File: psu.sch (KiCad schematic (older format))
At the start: 13 parts

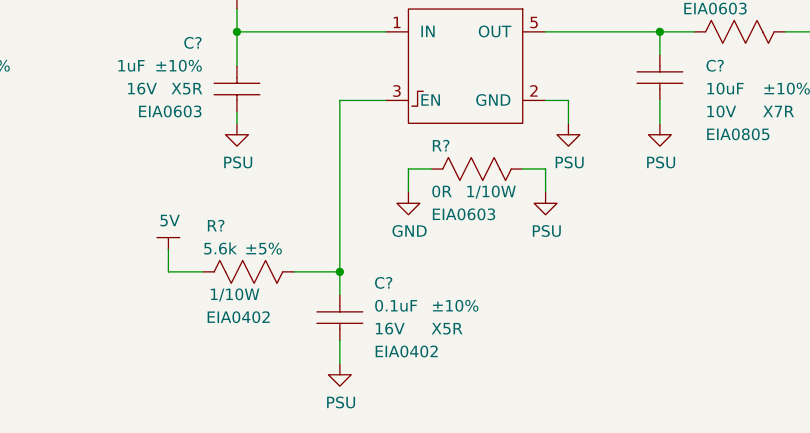
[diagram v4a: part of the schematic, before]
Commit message: Update ceramic capacitors with Vendor, Vendor_Pn, Fit fields following master library update.
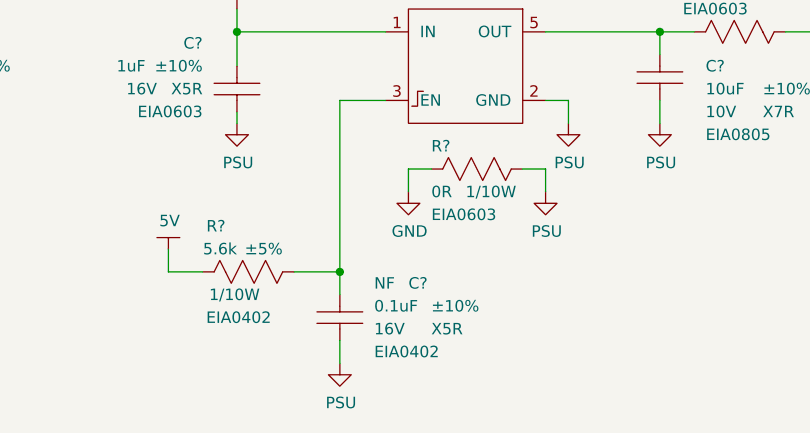
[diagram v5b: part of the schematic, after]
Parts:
- C? (x2): Digi-Key_PN 399-C0603C105K4PAC7411CT-ND -> (none); Fit (none) -> Yes; Vendor (none) -> Digikey; Vendor_PN (none) -> 399-C0603C105K4PAC7411CT-ND
- C?: Digi-Key_PN 399-14941-1-ND -> (none); Fit (none) -> Yes; Vendor (none) -> Digikey; Vendor_PN (none) -> 399-14941-1-ND
- C?: Digi-Key_PN 399-7411-1-ND -> (none); Fit (none) -> Yes; Vendor (none) -> Digikey; Vendor_PN (none) -> 399-7411-1-ND
- C?: Digi-Key_PN 399-7762-1-ND -> (none); Fit (none) -> NF; Vendor (none) -> Digikey; Vendor_PN (none) -> 399-7762-1-ND
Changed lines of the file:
@@
 F 2 "footprints_generic:CAPC160X80X95L35N" H 1700 6300 50  0001 L CNN
 F 3 "https://api.kemet.com/component-edge/download/specsheet/C0603C105K4PAC7411.pdf" H 1700 6400 50  0001 L CNN
-F 4 "399-C0603C105K4PAC7411CT-ND" H 5400 2950 50  0001 L CNN "Digi-Key_PN"
-F 5 "KEMET" H 5400 2850 50  0001 L CNN "Manufacturer"
-F 6 "C0603C105K4PAC7411" H 5400 2750 50  0001 L CNN "MPN"
-F 7 "Capacitors" H 1700 6700 50  0001 L CNN "Category"
-F 8 "Ceramic Capacitors" H 1700 6800 50  0001 L CNN "Family"
-F 9 "1uF" V 4900 2100 50  0000 L CNN "Capacitance"
-F 10 "±10%" V 4900 2300 50  0000 L CNN "Tolerance"
-F 11 "16V" V 5000 2100 50  0000 L CNN "Voltage"
-F 12 "X5R" V 5000 2300 50  0000 L CNN "Dielectric"
-F 13 "EIA0603" V 5100 2100 50  0000 L CNN "Package"
+F 4 "Digikey" H 5000 1950 50  0001 L CNN "Vendor"
+F 5 "399-C0603C105K4PAC7411CT-ND" H 5000 1950 50  0001 L CNN "Vendor_PN"
+F 6 "KEMET" H 5400 2850 50  0001 L CNN "Manufacturer"
+F 7 "C0603C105K4PAC7411" H 5400 2750 50  0001 L CNN "MPN"
+F 8 "Capacitors" H 1700 6700 50  0001 L CNN "Category"
+F 9 "Ceramic Capacitors" H 1700 6800 50  0001 L CNN "Family"
+F 10 "Yes" H 5000 1950 50  0001 L CNN "Fit"
+F 11 "1uF" V 4900 2100 50  0000 L CNN "Capacitance"
+F 12 "±10%" V 4900 2300 50  0000 L CNN "Tolerance"
+F 13 "16V" V 5000 2100 50  0000 L CNN "Voltage"
+F 14 "X5R" V 5000 2300 50  0000 L CNN "Dielectric"
+F 15 "EIA0603" V 5100 2100 50  0000 L CNN "Package"
 	1    5000 1950
 	0    1    1    0
@@
 F 2 "footprints_generic:CAPC160X80X95L35N" H 2500 6300 50  0001 L CNN
 F 3 "https://api.kemet.com/component-edge/download/datasheet/C0603C104K4PAC7867.pdf" H 2500 6400 50  0001 L CNN
-F 4 "399-14941-1-ND" H 6200 2950 50  0001 L CNN "Digi-Key_PN"
-F 5 "KEMET" H 6200 2850 50  0001 L CNN "Manufacturer"
-F 6 "C0603C104K4PAC7867" H 6200 2750 50  0001 L CNN "MPN"
-F 7 "Capacitors" H 2500 6700 50  0001 L CNN "Category"
-F 8 "Ceramic Capacitors" H 2500 6800 50  0001 L CNN "Family"
-F 9 "0.1uF" V 5700 2100 50  0000 L CNN "Capacitance"
-F 10 "±10%" V 5700 2350 50  0000 L CNN "Tolerance"
-F 11 "16V" V 5800 2100 50  0000 L CNN "Voltage"
-F 12 "X5R" V 5800 2350 50  0000 L CNN "Dielectric"
-F 13 "EIA0603" V 5900 2100 50  0000 L CNN "Package"
+F 4 "Digikey" H 5800 1950 50  0001 L CNN "Vendor"
+F 5 "399-14941-1-ND" H 5800 1950 50  0001 L CNN "Vendor_PN"
+F 6 "KEMET" H 6200 2850 50  0001 L CNN "Manufacturer"
+F 7 "C0603C104K4PAC7867" H 6200 2750 50  0001 L CNN "MPN"
+F 8 "Capacitors" H 2500 6700 50  0001 L CNN "Category"
+F 9 "Ceramic Capacitors" H 2500 6800 50  0001 L CNN "Family"
+F 10 "Yes" H 5800 1950 50  0001 L CNN "Fit"
+F 11 "0.1uF" V 5700 2100 50  0000 L CNN "Capacitance"
+F 12 "±10%" V 5700 2350 50  0000 L CNN "Tolerance"
+F 13 "16V" V 5800 2100 50  0000 L CNN "Voltage"
+F 14 "X5R" V 5800 2350 50  0000 L CNN "Dielectric"
+F 15 "EIA0603" V 5900 2100 50  0000 L CNN "Package"
 	1    5800 1950
 	0    1    1    0
@@
 F 2 "footprints_generic:CAPC200X125X110L50N" H 5950 6250 50  0001 L CNN
 F 3 "https://www.kemet.com/specsheet/C0805C106K8RACTU" H 5950 6350 50  0001 L CNN
-F 4 "399-7411-1-ND" H 9650 2900 50  0001 L CNN "Digi-Key_PN"
-F 5 "KEMET" H 9650 2800 50  0001 L CNN "Manufacturer"
-F 6 "C0805C106K8RACTU" H 9650 2700 50  0001 L CNN "MPN"
-F 7 "Capacitors" H 5950 6650 50  0001 L CNN "Category"
-F 8 "Ceramic Capacitors" H 5950 6750 50  0001 L CNN "Family"
-F 9 "10uF" V 9300 2100 50  0000 L CNN "Capacitance"
-F 10 "±10%" V 9300 2350 50  0000 L CNN "Tolerance"
-F 11 "10V" V 9400 2100 50  0000 L CNN "Voltage"
-F 12 "X7R" V 9400 2350 50  0000 L CNN "Dielectric"
-F 13 "EIA0805" V 9500 2100 50  0000 L CNN "Package"
+F 4 "Digikey" H 9250 1900 50  0001 L CNN "Vendor"
+F 5 "399-7411-1-ND" H 9250 1900 50  0001 L CNN "Vendor_PN"
+F 6 "KEMET" H 9650 2800 50  0001 L CNN "Manufacturer"
+F 7 "C0805C106K8RACTU" H 9650 2700 50  0001 L CNN "MPN"
+F 8 "Capacitors" H 5950 6650 50  0001 L CNN "Category"
+F 9 "Ceramic Capacitors" H 5950 6750 50  0001 L CNN "Family"
+F 10 "Yes" H 9250 1900 50  0001 L CNN "Fit"
+F 11 "10uF" V 9300 2100 50  0000 L CNN "Capacitance"
+F 12 "±10%" V 9300 2350 50  0000 L CNN "Tolerance"
+F 13 "10V" V 9400 2100 50  0000 L CNN "Voltage"
+F 14 "X7R" V 9400 2350 50  0000 L CNN "Dielectric"
+F 15 "EIA0805" V 9500 2100 50  0000 L CNN "Package"
 	1    9250 1900
 	0    1    1    0
@@
 U 1 1 60483D8C
 P 7850 2950
-F 0 "C?" V 7700 3100 50  0000 L CNN
+F 0 "C?" V 7700 3250 50  0000 L CNN
 F 1 "CAP-EIA0402" H 8250 4050 50  0001 L CNN
 F 2 "footprints_generic:CAPC100X50X55L30N" H 4550 7300 50  0001 L CNN
 F 3 "https://api.kemet.com/component-edge/download/datasheet/C0402C104K4PACTU.pdf" H 4550 7400 50  0001 L CNN
-F 4 "399-7762-1-ND" H 8250 3950 50  0001 L CNN "Digi-Key_PN"
-F 5 "KEMET" H 8250 3850 50  0001 L CNN "Manufacturer"
-F 6 "C0402C104K4PACTU" H 8250 3750 50  0001 L CNN "MPN"
-F 7 "Capacitors" H 4550 7700 50  0001 L CNN "Category"
-F 8 "Ceramic Capacitors" H 4550 7800 50  0001 L CNN "Family"
-F 9 "0.1uF" V 7800 3100 50  0000 L CNN "Capacitance"
-F 10 "±10%" V 7800 3350 50  0000 L CNN "Tolerance"
-F 11 "16V" V 7900 3100 50  0000 L CNN "Voltage"
-F 12 "X5R" V 7900 3350 50  0000 L CNN "Dielectric"
-F 13 "EIA0402" V 8000 3100 50  0000 L CNN "Package"
+F 4 "Digikey" H 7850 2950 50  0001 L CNN "Vendor"
+F 5 "399-7762-1-ND" H 7850 2950 50  0001 L CNN "Vendor_PN"
+F 6 "KEMET" H 8250 3850 50  0001 L CNN "Manufacturer"
+F 7 "C0402C104K4PACTU" H 8250 3750 50  0001 L CNN "MPN"
+F 8 "Capacitors" H 4550 7700 50  0001 L CNN "Category"
+F 9 "Ceramic Capacitors" H 4550 7800 50  0001 L CNN "Family"
+F 10 "NF" V 7700 3100 50  0000 L CNN "Fit"
+F 11 "0.1uF" V 7800 3100 50  0000 L CNN "Capacitance"
+F 12 "±10%" V 7800 3350 50  0000 L CNN "Tolerance"
+F 13 "16V" V 7900 3100 50  0000 L CNN "Voltage"
+F 14 "X5R" V 7900 3350 50  0000 L CNN "Dielectric"
+F 15 "EIA0402" V 8000 3100 50  0000 L CNN "Package"
 	1    7850 2950
 	0    1    1    0
@@
 F 2 "footprints_generic:CAPC160X80X95L35N" H 4100 6300 50  0001 L CNN
 F 3 "https://api.kemet.com/component-edge/download/specsheet/C0603C105K4PAC7411.pdf" H 4100 6400 50  0001 L CNN
-F 4 "399-C0603C105K4PAC7411CT-ND" H 7800 2950 50  0001 L CNN "Digi-Key_PN"
-F 5 "KEMET" H 7800 2850 50  0001 L CNN "Manufacturer"
-F 6 "C0603C105K4PAC7411" H 7800 2750 50  0001 L CNN "MPN"
-F 7 "Capacitors" H 4100 6700 50  0001 L CNN "Category"
-F 8 "Ceramic Capacitors" H 4100 6800 50  0001 L CNN "Family"
-F 9 "1uF" V 7300 1550 50  0000 R CNN "Capacitance"
-F 10 "±10%" V 7300 1800 50  0000 R CNN "Tolerance"
-F 11 "16V" V 7400 1600 50  0000 R CNN "Voltage"
-F 12 "X5R" V 7400 1800 50  0000 R CNN "Dielectric"
-F 13 "EIA0603" V 7500 1800 50  0000 R CNN "Package"
+F 4 "Digikey" H 7400 1950 50  0001 L CNN "Vendor"
+F 5 "399-C0603C105K4PAC7411CT-ND" H 7400 1950 50  0001 L CNN "Vendor_PN"
+F 6 "KEMET" H 7800 2850 50  0001 L CNN "Manufacturer"
+F 7 "C0603C105K4PAC7411" H 7800 2750 50  0001 L CNN "MPN"
+F 8 "Capacitors" H 4100 6700 50  0001 L CNN "Category"
+F 9 "Ceramic Capacitors" H 4100 6800 50  0001 L CNN "Family"
+F 10 "Yes" H 7400 1950 50  0001 R CNN "Fit"
+F 11 "1uF" V 7300 1550 50  0000 R CNN "Capacitance"
+F 12 "±10%" V 7300 1800 50  0000 R CNN "Tolerance"
+F 13 "16V" V 7400 1600 50  0000 R CNN "Voltage"
+F 14 "X5R" V 7400 1800 50  0000 R CNN "Dielectric"
+F 15 "EIA0603" V 7500 1800 50  0000 R CNN "Package"
 	1    7400 1950
 	0    1    1    0

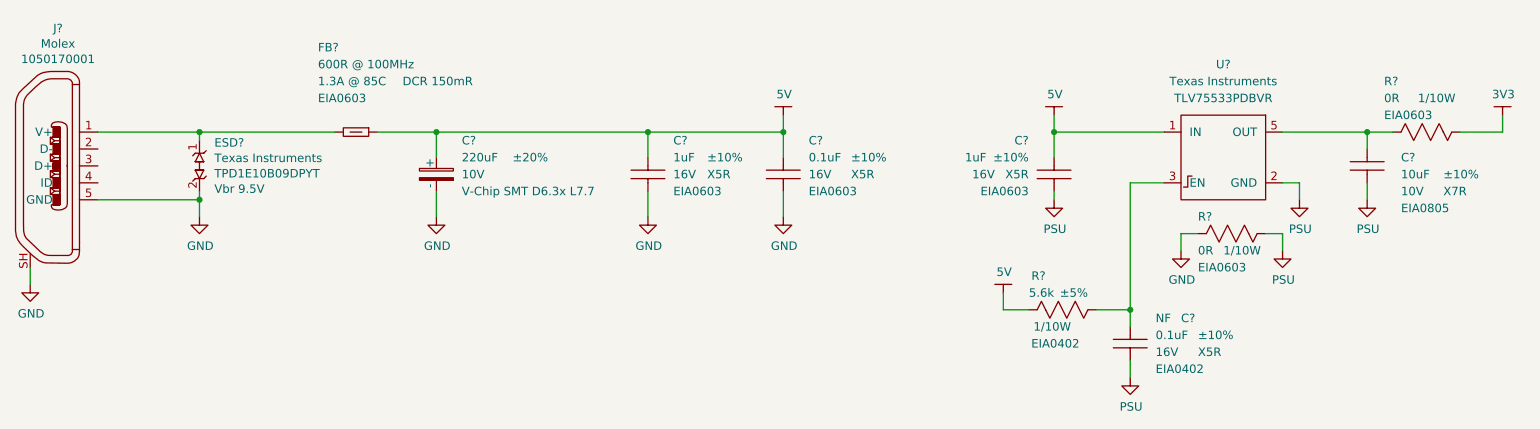
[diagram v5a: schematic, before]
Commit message: Update symbols in psu.sch with Vendor, Vendor_PN, Fit fields.
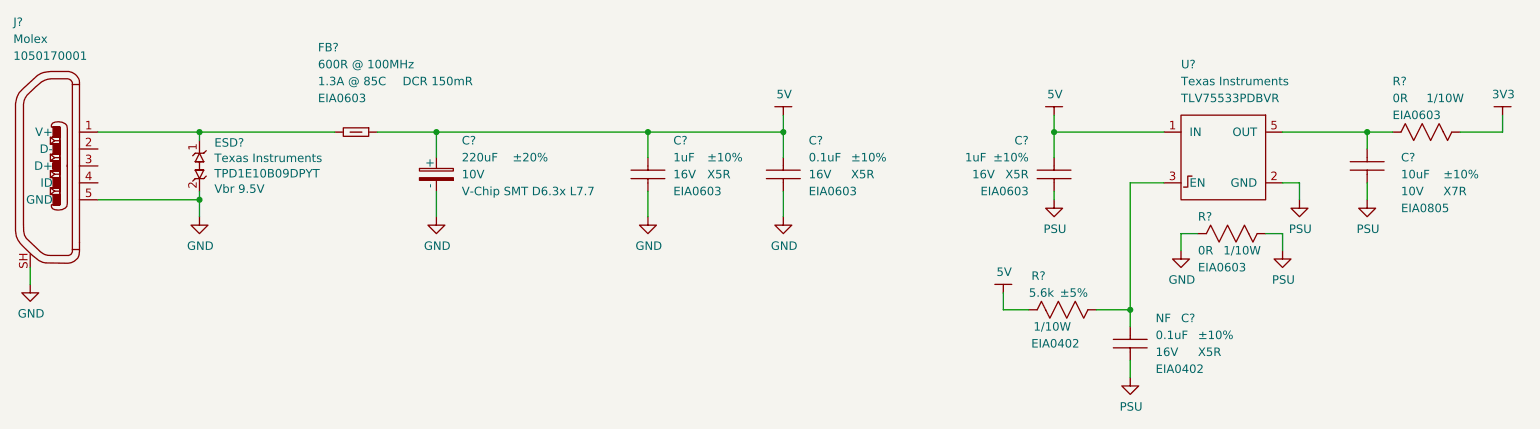
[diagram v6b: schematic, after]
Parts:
- removed R?: RES-EIA0603, footprints_generic:RESC160X85X55L30N, symbol gz_Chip-Resistors-Surface-Mount:RES-EIA0603
- added R?: RES-EIA0603, footprints_generic:RESC160X85X55L30N, symbol gz_Chip-Resistors-Surface-Mount:RES-EIA0603
- C?: Digi-Key_PN 732-8492-1-ND -> (none); Fit (none) -> Yes; Vendor (none) -> Digikey; Vendor_PN (none) -> 732-8492-1-ND
- FB?: Digi-Key_PN 490-5258-1-ND -> (none); Fit (none) -> Yes; Vendor (none) -> Digikey; Vendor_PN (none) -> 490-5258-1-ND
- J?: Digi-Key_PN WM1399CT-ND -> (none); Fit (none) -> Yes; Vendor (none) -> Digikey; Vendor_PN (none) -> WM1399CT-ND
- R?: Digi-Key_PN P0.0GCT-ND -> (none); Fit (none) -> Yes; Vendor (none) -> Digikey; Vendor_PN (none) -> P0.0GCT-ND
- R?: Digi-Key_PN P5.6KJCT-ND -> (none); Fit (none) -> Yes; Vendor (none) -> Digikey; Vendor_PN (none) -> P5.6KJCT-ND
- U?: Digi-Key_PN 296-50411-1-ND -> (none); Fit (none) -> Yes; Vendor (none) -> Digikey; Vendor_PN (none) -> 296-50411-1-ND
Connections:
- net +3V3: now also R?.2
- net at C?.1, U?.5 (OUT): now also R?.1

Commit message: Update footprint ref in Molex USB connector.
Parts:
- J?: footprint gz-connectors:Molex-1050170001 -> footprints:Molex-1050170001
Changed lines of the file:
@@
 F 0 "J?" H 1250 2750 50  0000 L CNN
 F 1 "Molex-1050170001" H 1950 2850 50  0001 L CNN
-F 2 "gz-connectors:Molex-1050170001" H 1950 2750 50  0001 L CNN
+F 2 "footprints:Molex-1050170001" H 1950 2750 50  0001 L CNN
 F 3 "https://www.molex.com/pdm_docs/sd/1050170001_sd.pdf" H 1650 2200 50  0001 L CNN
 F 4 "Digikey" H 1450 1900 50  0001 L CNN "Vendor"

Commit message: Update schematic to KEMET and Panasonic passives.
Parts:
- C? (x2): MPN C0603C105K4PAC7411 -> C0603C105K4PACTU; Vendor_PN 399-C0603C105K4PAC7411CT-ND -> 399-5090-1-ND
- C?: MPN C0603C104K4PAC7867 -> C0603C104K4PACTU
- ESD?: Fit Y -> Yes
- R?: Voltage 50V -> N/A
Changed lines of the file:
@@
 F 1 "Molex-1050170001" H 1950 2850 50  0001 L CNN
 F 2 "footprints:Molex-1050170001" H 1950 2750 50  0001 L CNN
-F 3 "https://www.molex.com/pdm_docs/sd/1050170001_sd.pdf" H 1650 2200 50  0001 L CNN
+F 3 "${DATASHEETS}/Molex-1050170001.pdf" H 1650 2200 50  0001 L CNN
 F 4 "Digikey" H 1450 1900 50  0001 L CNN "Vendor"
 F 5 "WM1399CT-ND" H 1450 1900 50  0001 L CNN "Vendor_PN"
@@
 F 1 "CAP-EIA0603" H 5400 3050 50  0001 L CNN
 F 2 "footprints_generic:CAPC160X80X95L35N" H 1700 6300 50  0001 L CNN
-F 3 "https://api.kemet.com/component-edge/download/specsheet/C0603C105K4PAC7411.pdf" H 1700 6400 50  0001 L CNN
+F 3 "${KEMET_MLCC_BASE}C0603C105K4PACTU" H 1700 6400 50  0001 L CNN
 F 4 "Digikey" H 5000 1950 50  0001 L CNN "Vendor"
-F 5 "399-C0603C105K4PAC7411CT-ND" H 5000 1950 50  0001 L CNN "Vendor_PN"
+F 5 "399-5090-1-ND" H 5000 1950 50  0001 L CNN "Vendor_PN"
 F 6 "KEMET" H 5400 2850 50  0001 L CNN "Manufacturer"
-F 7 "C0603C105K4PAC7411" H 5400 2750 50  0001 L CNN "MPN"
+F 7 "C0603C105K4PACTU" H 5400 2750 50  0001 L CNN "MPN"
 F 8 "Capacitors" H 1700 6700 50  0001 L CNN "Category"
 F 9 "Ceramic Capacitors" H 1700 6800 50  0001 L CNN "Family"
@@
 F 1 "CAP-EIA0603" H 6200 3050 50  0001 L CNN
 F 2 "footprints_generic:CAPC160X80X95L35N" H 2500 6300 50  0001 L CNN
-F 3 "https://api.kemet.com/component-edge/download/datasheet/C0603C104K4PAC7867.pdf" H 2500 6400 50  0001 L CNN
+F 3 "${KEMET_MLCC_BASE}C0603C104K4PACTU" H 2500 6400 50  0001 L CNN
 F 4 "Digikey" H 5800 1950 50  0001 L CNN "Vendor"
 F 5 "399-14941-1-ND" H 5800 1950 50  0001 L CNN "Vendor_PN"
 F 6 "KEMET" H 6200 2850 50  0001 L CNN "Manufacturer"
-F 7 "C0603C104K4PAC7867" H 6200 2750 50  0001 L CNN "MPN"
+F 7 "C0603C104K4PACTU" H 6200 2750 50  0001 L CNN "MPN"
 F 8 "Capacitors" H 2500 6700 50  0001 L CNN "Category"
 F 9 "Ceramic Capacitors" H 2500 6800 50  0001 L CNN "Family"
@@
 F 1 "CAP-EIA0805" H 9650 3000 50  0001 L CNN
 F 2 "footprints_generic:CAPC200X125X110L50N" H 5950 6250 50  0001 L CNN
-F 3 "https://www.kemet.com/specsheet/C0805C106K8RACTU" H 5950 6350 50  0001 L CNN
+F 3 "${KEMET_MLCC_BASE}C0805C106K8RACTU" H 5950 6350 50  0001 L CNN
 F 4 "Digikey" H 9250 1900 50  0001 L CNN "Vendor"
 F 5 "399-7411-1-ND" H 9250 1900 50  0001 L CNN "Vendor_PN"
@@
 F 1 "RES-EIA0603" H 9250 3200 50  0001 L CNN
 F 2 "footprints_generic:RESC160X85X55L30N" H 5150 6650 50  0001 L CNN
-F 3 "http://industrial.panasonic.com/www-cgi/jvcr13pz.cgi?E+PZ+3+AOA0001+ERJ3GEY0R00V+7+WW" H 5150 6750 50  0001 L CNN
+F 3 "${PANASONIC_GP_CHIP_RES_BASE}ERJ3GEY0R00V" H 5150 6750 50  0001 L CNN
 F 4 "Digikey" H 8450 2300 50  0001 L CNN "Vendor"
 F 5 "P0.0GCT-ND" H 8450 2300 50  0001 L CNN "Vendor_PN"
@@
 F 1 "CAP-EIA0402" H 8250 4050 50  0001 L CNN
 F 2 "footprints_generic:CAPC100X50X55L30N" H 4550 7300 50  0001 L CNN
-F 3 "https://api.kemet.com/component-edge/download/datasheet/C0402C104K4PACTU.pdf" H 4550 7400 50  0001 L CNN
+F 3 "${KEMET_MLCC_BASE}C0402C104K4PACTU" H 4550 7400 50  0001 L CNN
 F 4 "Digikey" H 7850 2950 50  0001 L CNN "Vendor"
 F 5 "399-7762-1-ND" H 7850 2950 50  0001 L CNN "Vendor_PN"
@@
 F 1 "RES-EIA0402" H 8250 3650 50  0001 L CNN
 F 2 "footprints_generic:RESC100X50X40L25NN" H 4150 7100 50  0001 L CNN
-F 3 "https://industrial.panasonic.com/ww/products/resistors/chip-resistors/general-purpose-chip-resistors/models/ERJ2GEJ562X" H 4150 7200 50  0001 L CNN
+F 3 "${PANASONIC_GP_CHIP_RES_BASE}ERJ2GEJ562X" H 4150 7200 50  0001 L CNN
 F 4 "Digikey" H 7450 2750 50  0001 L CNN "Vendor"
 F 5 "P5.6KJCT-ND" H 7450 2750 50  0001 L CNN "Vendor_PN"
@@
 F 12 "±5%" H 7300 2650 50  0000 L CNN "Tolerance"
 F 13 "1/10W" H 7400 2850 50  0000 L CNN "Power"
-F 14 "50V" V 7586 2828 50  0001 L CNN "Voltage"
+F 14 "N/A" V 7586 2828 50  0001 L CNN "Voltage"
 F 15 "EIA0402" H 7350 2950 50  0000 L CNN "Package"
 	1    7450 2750
@@
 F 1 "CAP-EIA0603" H 7800 3050 50  0001 L CNN
 F 2 "footprints_generic:CAPC160X80X95L35N" H 4100 6300 50  0001 L CNN
-F 3 "https://api.kemet.com/component-edge/download/specsheet/C0603C105K4PAC7411.pdf" H 4100 6400 50  0001 L CNN
+F 3 "${KEMET_MLCC_BASE}C0603C105K4PACTU" H 4100 6400 50  0001 L CNN
 F 4 "Digikey" H 7400 1950 50  0001 L CNN "Vendor"
-F 5 "399-C0603C105K4PAC7411CT-ND" H 7400 1950 50  0001 L CNN "Vendor_PN"
+F 5 "399-5090-1-ND" H 7400 1950 50  0001 L CNN "Vendor_PN"
 F 6 "KEMET" H 7800 2850 50  0001 L CNN "Manufacturer"
-F 7 "C0603C105K4PAC7411" H 7800 2750 50  0001 L CNN "MPN"
+F 7 "C0603C105K4PACTU" H 7800 2750 50  0001 L CNN "MPN"
 F 8 "Capacitors" H 4100 6700 50  0001 L CNN "Category"
 F 9 "Ceramic Capacitors" H 4100 6800 50  0001 L CNN "Family"
@@
 F 8 "Circuit protection" H 3150 2600 50  0001 L CNN "Category"
 F 9 "TVS - Diodes" H 3150 2500 50  0001 L CNN "Family"
-F 10 "Y" H 2800 2050 50  0001 L CNN "Fit"
+F 10 "Yes" H 2800 2050 50  0001 L CNN "Fit"
 F 11 "Vbr 9.5V" H 2438 1764 50  0000 L CNN "Breakdown Voltage"
 F 12 "EIA0402" H 3150 2400 50  0001 L CNN "Package"
@@
 F 1 "RES-EIA0603" H 10400 2600 50  0001 L CNN
 F 2 "footprints_generic:RESC160X85X55L30N" H 6300 6050 50  0001 L CNN
-F 3 "http://industrial.panasonic.com/www-cgi/jvcr13pz.cgi?E+PZ+3+AOA0001+ERJ3GEY0R00V+7+WW" H 6300 6150 50  0001 L CNN
+F 3 "${PANASONIC_GP_CHIP_RES_BASE}ERJ3GEY0R00V" H 6300 6150 50  0001 L CNN
 F 4 "Digikey" H 9600 1700 50  0001 L CNN "Vendor"
 F 5 "P0.0GCT-ND" H 9600 1700 50  0001 L CNN "Vendor_PN"
